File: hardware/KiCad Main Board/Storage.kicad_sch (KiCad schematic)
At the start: 14 parts, among them J4 MEM2061-01-188-00-A_REVA, U5 MX25L25645GM2I-08G

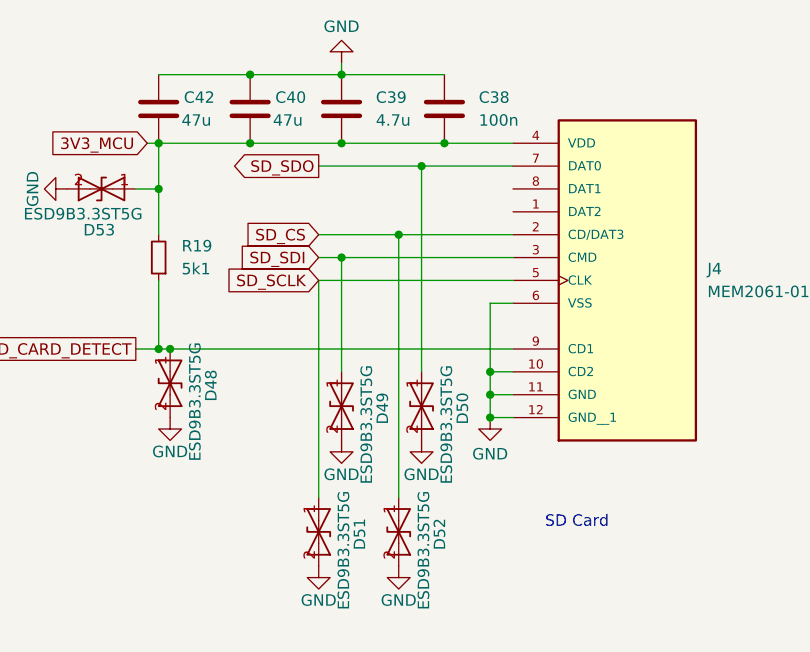
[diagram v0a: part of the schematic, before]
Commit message: added separate project for the radio board, re-organised hardware folder
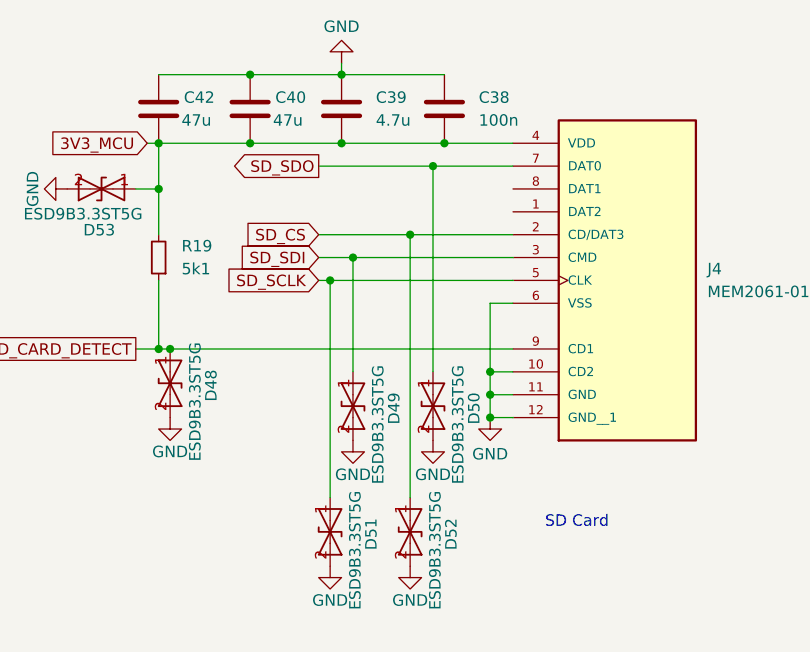
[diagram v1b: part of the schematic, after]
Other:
- moved on the sheet: D49, D50, D51, D52

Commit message: working on PCB
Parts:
- J4: footprint MEM2061-01-188-00-A_REVA:GCT_MEM2061-01-188-00-A_REVA -> MEM2061:GCT_MEM2061-01-188-00-A_REVA
- R19: footprint (none) -> Resistor_SMD:R_0603_1608Metric_Pad0.98x0.95mm_HandSolder
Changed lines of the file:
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@@
 			)
 		)
-		(property "Footprint" ""
+		(property "Footprint" "Resistor_SMD:R_0603_1608Metric_Pad0.98x0.95mm_HandSolder"
 			(at 186.69 52.07 0)
 			(effects
@@
 			)
 		)
-		(property "Footprint" "MEM2061-01-188-00-A_REVA:GCT_MEM2061-01-188-00-A_REVA"
+		(property "Footprint" "MEM2061:GCT_MEM2061-01-188-00-A_REVA"
 			(at 231.14 52.07 0)
 			(effects
